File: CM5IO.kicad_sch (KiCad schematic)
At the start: 18 parts, among them J11 USB_C_Receptacle_USB2.0, J4 ATX-24, Q1 MMBT7002K, Q2 DMP3013SFV-7

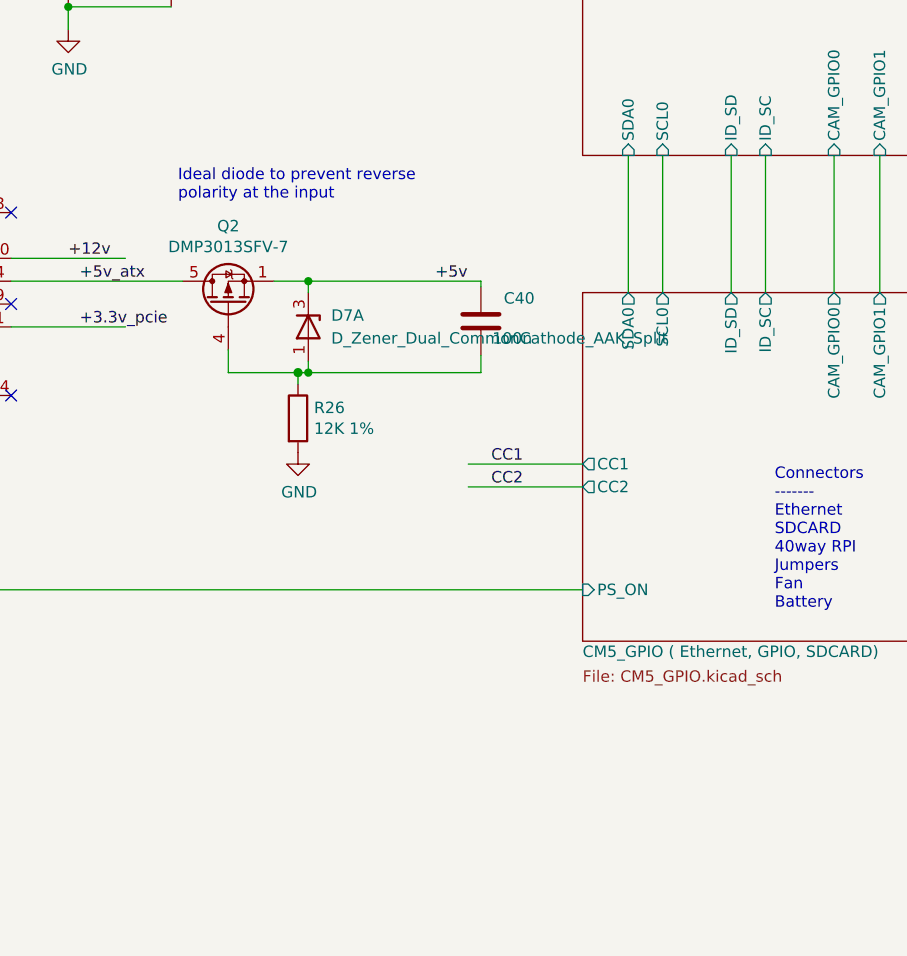
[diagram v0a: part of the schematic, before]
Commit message: add dummy pad and more ideal ideal diode
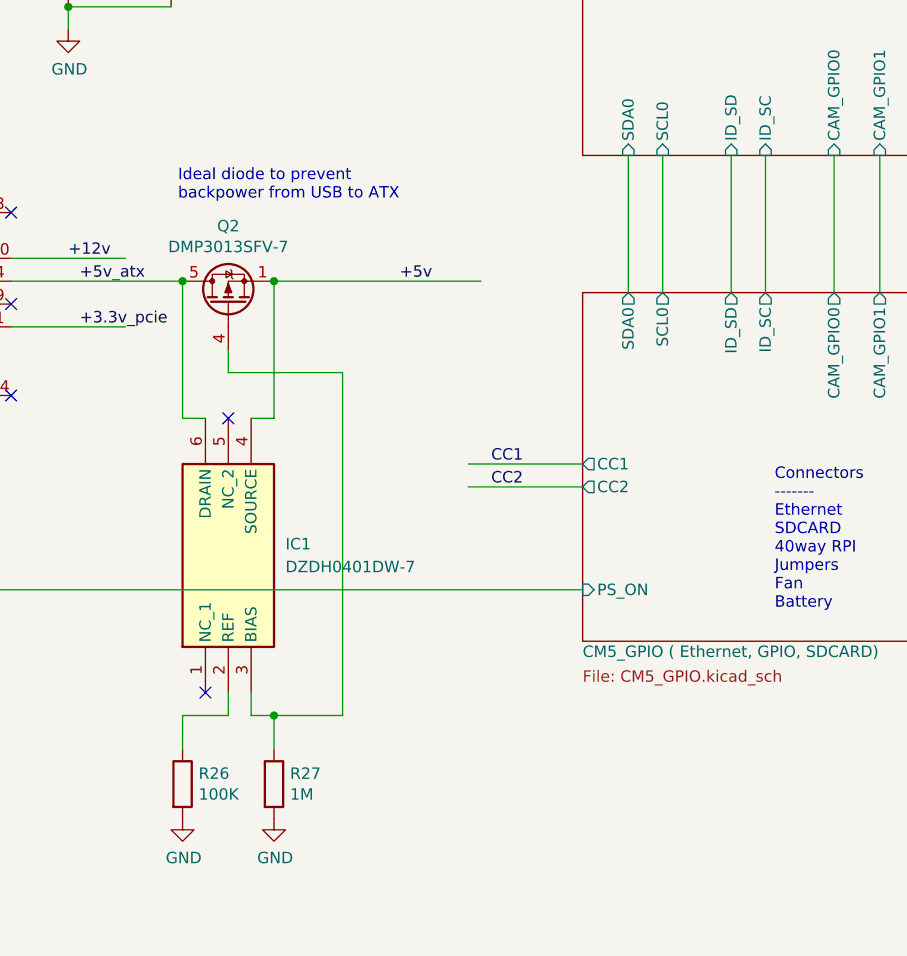
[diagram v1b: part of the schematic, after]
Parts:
- removed C40: 100n, Capacitor_SMD:C_0402_1005Metric, symbol Device:C
- removed D7: D_Zener_Dual_CommonCathode_AAK_Split, Package_TO_SOT_SMD:SOT-23, symbol Device:D_Zener_Dual_CommonCathode_AAK_Split
- added IC1: DZDH0401DW-7, Package_TO_SOT_SMD:SOT-363_SC-70-6, symbol CM5IO:DZDH0401DW-7
- added R27: 1M, Resistor_SMD:R_0402_1005Metric, symbol Device:R
- R26: value 12K 1% -> 100K
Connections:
- net +5v: now also IC1.4 (SOURCE)
- net +5v_atx: now also IC1.6 (DRAIN)
- net GND: now also R27.2
- net at R26.1: now also IC1.2 (REF); no longer Q2.4 (G)
- new net: IC1.3 (BIAS), Q2.4 (G), R27.1
- no-connect marks 5 -> 7
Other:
- note added: "Ideal diode to prevent backpower from USB to ATX"
- note removed: "Ideal diode to prevent reverse polarity at the input"
- moved on the sheet: R26
